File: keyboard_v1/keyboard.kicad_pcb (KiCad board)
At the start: 2 copper layers, 205.5 x 64.2 mm, 112 parts, among them J1 BOOT0, J2 SWD, J3 UART, J4 rs485, SW1 SW_Push, SW10 SW_Push, SW11 SW_Push, SW12 SW_Push, SW13 SW_Push, SW14 SW_Push, SW15 SW_Push, SW16 SW_Push, SW17 SW_Push, SW18 SW_Push, SW19 SW_Push, SW2 SW_Push, SW20 SW_Push, SW21 SW_Push, SW22 SW_Push, SW23 SW_Push, SW24 SW_Push, SW25 SW_Push, SW26 SW_Push, SW27 SW_Push, SW28 SW_Push, SW29 SW_Push, SW3 SW_Push, SW30 SW_Push, SW31 SW_Push, SW4 SW_Push, SW5 SW_Push, SW6 SW_Push, SW7 SW_Push, SW8 SW_Push, SW9 SW_Push, U1 STM32F030C8Tx, U2 74HC595, U3 SP3485EN, Y1 X322516MLB4SI

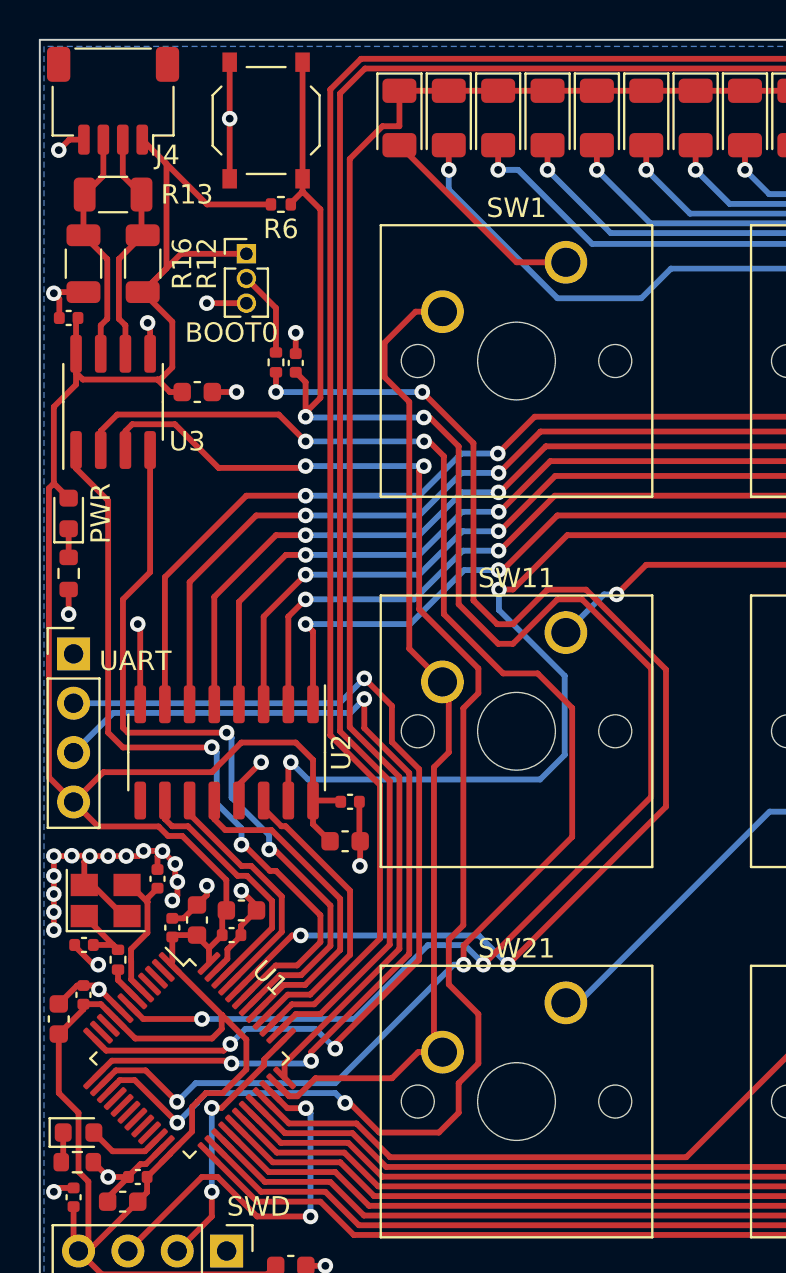
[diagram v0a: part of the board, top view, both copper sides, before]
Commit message: remove boot selector on keyboard
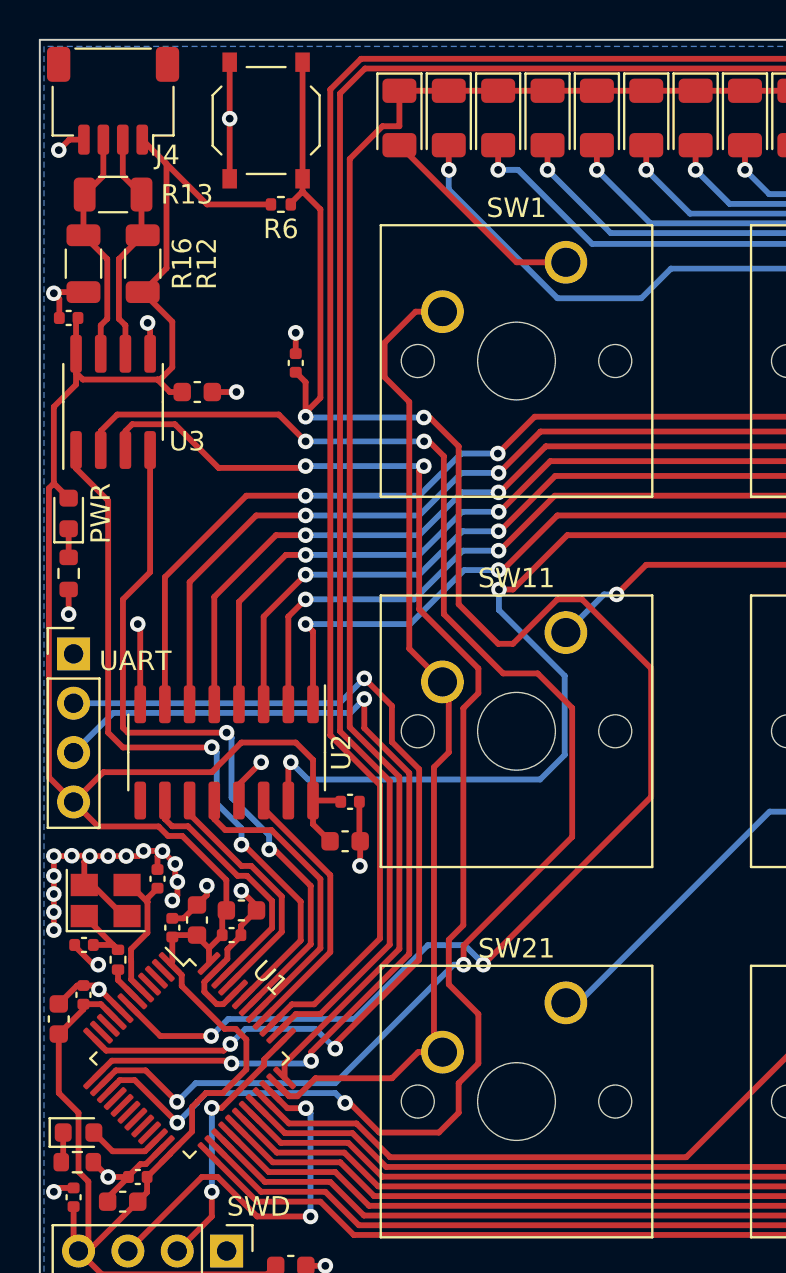
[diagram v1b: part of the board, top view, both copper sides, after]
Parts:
- removed J1: BOOT0, Connector_PinHeader_1.27mm:PinHeader_1x03_P1.27mm_Vertical
- removed R11: 10k, Resistor_SMD:R_0402_1005Metric
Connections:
- U1 pad 44: /BOOT0_JMP -> GND
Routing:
- net /BOOT0_JMP: track 67.5 -> 0.00 mm, vias 4 -> 0
- net +3.3V: track 155.5 -> 142.9 mm
- net Net-(J1-Pin_2): track 4.44 -> 0.00 mm
- net RS485_RO: track 38.6 -> 37.0 mm
- net LED_SER: track 15.7 -> 14.0 mm
- net GND: track 79.2 -> 80.7 mm, vias 40 -> 39
- net RS485_DI: track 39.0 -> 37.5 mm
- net LED_RCLK: track 17.3 -> 15.9 mm
- net Net-(U1-NRST): track 91.5 -> 92.2 mm

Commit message: keyboard PCB updates
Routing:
- net ROW0: track 78.7 -> 79.4 mm
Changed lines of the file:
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@@
   (segment (start 86.36 55.62) (end 83.82 55.62) (width 0.3) (layer "F.Cu") (net 56))
   (segment (start 68.58 55.62) (end 66.04 55.62) (width 0.3) (layer "F.Cu") (net 56))
-  (segment (start 62.62647 57.445) (end 60.944 59.12747) (width 0.3) (layer "F.Cu") (net 56))
-  (segment (start 60.944 88.369116) (end 63.5 90.925116) (width 0.3) (layer "F.Cu") (net 56))
+  (segment (start 61.474 55.62) (end 60.944 56.15) (width 0.3) (layer "F.Cu") (net 56))
   (segment (start 83.82 55.62) (end 81.28 55.62) (width 0.3) (layer "F.Cu") (net 56))
-  (segment (start 63.5 55.62) (end 63.5 57.445) (width 0.3) (layer "F.Cu") (net 56))
-  (segment (start 60.944 59.12747) (end 60.944 88.369116) (width 0.3) (layer "F.Cu") (net 56))
+  (segment (start 63.5 55.62) (end 61.474 55.62) (width 0.3) (layer "F.Cu") (net 56))
   (segment (start 66.04 55.62) (end 63.5 55.62) (width 0.3) (layer "F.Cu") (net 56))
   (segment (start 63.5 90.925116) (end 63.5 99.767106) (width 0.3) (layer "F.Cu") (net 56))
+  (segment (start 60.944 88.369116) (end 63.5 90.925116) (width 0.3) (layer "F.Cu") (net 56))
   (segment (start 81.28 55.62) (end 78.74 55.62) (width 0.3) (layer "F.Cu") (net 56))
+  (segment (start 63.5 99.767106) (end 57.592876 105.67423) (width 0.3) (layer "F.Cu") (net 56))
   (segment (start 76.2 55.62) (end 73.66 55.62) (width 0.3) (layer "F.Cu") (net 56))
+  (segment (start 60.944 56.15) (end 60.944 88.369116) (width 0.3) (layer "F.Cu") (net 56))
   (segment (start 78.74 55.62) (end 76.2 55.62) (width 0.3) (layer "F.Cu") (net 56))
+  (segment (start 73.66 55.62) (end 71.12 55.62) (width 0.3) (layer "F.Cu") (net 56))
   (segment (start 57.592876 105.67423) (end 57.592876 106.408788) (width 0.3) (layer "F.Cu") (net 56))
-  (segment (start 63.5 57.445) (end 62.62647 57.445) (width 0.3) (layer "F.Cu") (net 56))
-  (segment (start 73.66 55.62) (end 71.12 55.62) (width 0.3) (layer "F.Cu") (net 56))
   (segment (start 71.12 55.62) (end 68.58 55.62) (width 0.3) (layer "F.Cu") (net 56))
-  (segment (start 63.5 99.767106) (end 57.592876 105.67423) (width 0.3) (layer "F.Cu") (net 56))
   (segment (start 104.14 55.62) (end 101.6 55.62) (width 0.3) (layer "F.Cu") (net 57))
   (segment (start 57.239322 104.057658) (end 58.17298 103.124) (width 0.3) (layer "F.Cu") (net 57))
